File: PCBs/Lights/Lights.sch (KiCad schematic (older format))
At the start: 6 parts

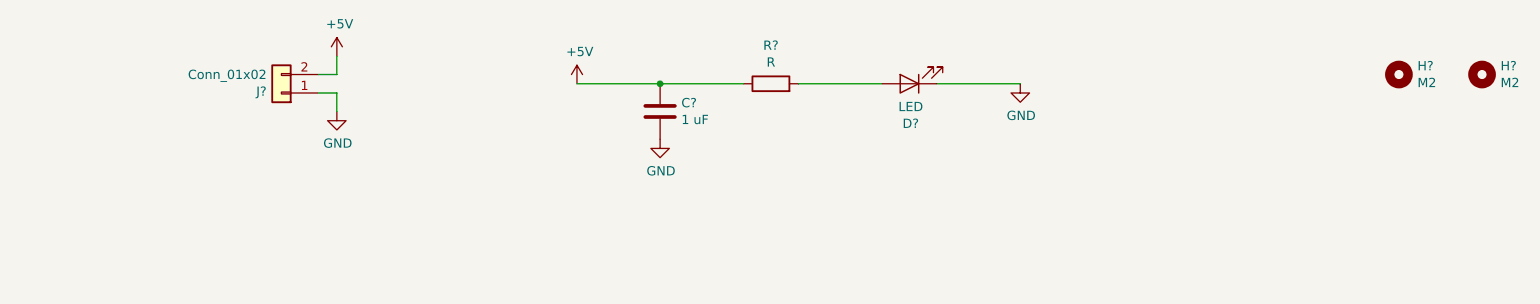
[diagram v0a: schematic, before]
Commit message: Schematic done
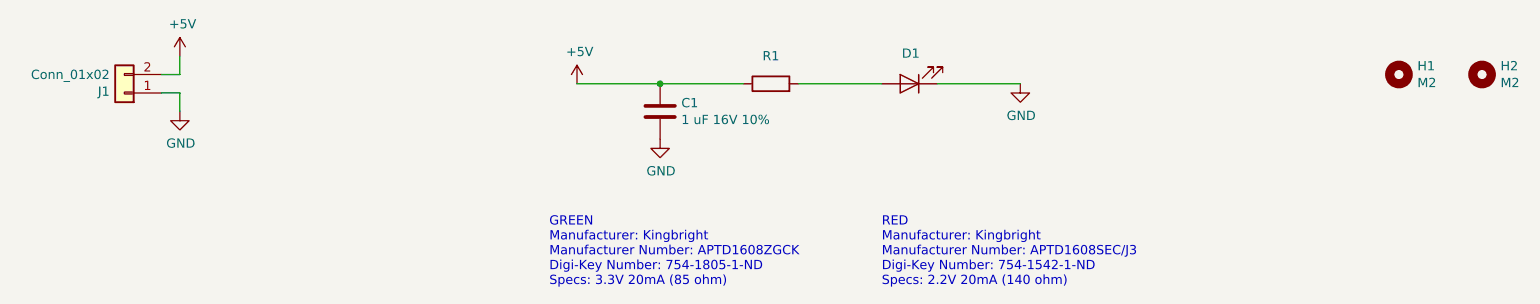
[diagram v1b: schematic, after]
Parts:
- C1: renamed from C?; value 1 uF -> 1 uF 16V 10%; footprint (none) -> Capacitor_SMD:C_0603_1608Metric_Pad1.05x0.95mm_HandSolder
- D1: renamed from D?; value LED -> See Notes; footprint (none) -> LED_SMD:LED_0603_1608Metric_Pad1.05x0.95mm_HandSolder
- J1: renamed from J?; footprint (none) -> Connector_JST:JST_GH_BM02B-GHS-TBT_1x02-1MP_P1.25mm_Vertical; Digi-Key # (none) -> 455-1578-1-ND; Digi-Key LinkDigi LinkDigi-Key Link (none) -> https://www.digikey.ca/en/products/detail/jst-sales-america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; Manufacturer (none) -> JST Sales America Inc.; Manufacturer # (none) -> BM02B-GHS-TBT(LF)(SN)(N)
- R1: renamed from R?; value R -> See Notes; footprint (none) -> Resistor_SMD:R_0603_1608Metric_Pad1.05x0.95mm_HandSolder
- gave numbers to parts that had none: 2
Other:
- note added: "GREEN\nManufacturer: Kingbright\nManufacturer Number: APTD1608ZGCK\nDigi-Key Number: 754-1805-1-ND\nSpecs: 3.3V 20mA (85 ohm)"
- note added: "RED\nManufacturer: Kingbright\nManufacturer Number: APTD1608SEC/J3\nDigi-Key Number: 754-1542-1-ND\nSpecs: 2.2V 20mA (140 ohm)"
- moved on the sheet: J1
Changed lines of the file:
@@
 EESchema Schematic File Version 4
+LIBS:Lights-cache
 EELAYER 30 0
 EELAYER END
@@
 $EndDescr
 $Comp
-L Connector_Generic:Conn_01x02 J?
+L Connector_Generic:Conn_01x02 J1
 U 1 1 5FF23492
-P 2700 4350
-F 0 "J?" H 2780 4342 50  0000 L CNN
-F 1 "Conn_01x02" H 2780 4251 50  0000 L CNN
-F 2 "" H 2700 4350 50  0001 C CNN
-F 3 "~" H 2700 4350 50  0001 C CNN
-	1    2700 4350
+P 1850 4350
+F 0 "J1" H 1930 4342 50  0000 L CNN
+F 1 "Conn_01x02" H 1930 4251 50  0000 L CNN
+F 2 "Connector_JST:JST_GH_BM02B-GHS-TBT_1x02-1MP_P1.25mm_Vertical" H 1850 4350 50  0001 C CNN
+F 3 "~" H 1850 4350 50  0001 C CNN
+F 4 "JST Sales America Inc." H 1850 4350 50  0001 C CNN "Manufacturer"
+F 5 "BM02B-GHS-TBT(LF)(SN)(N)" H 1850 4350 50  0001 C CNN "Manufacturer #"
+F 6 "455-1578-1-ND" H 1850 4350 50  0001 C CNN "Digi-Key #"
+F 7 "https://www.digikey.ca/en/products/detail/jst-sales-america-inc/BM02B-GHS-TBT-LF-SN-N/807800" H 1850 4350 50  0001 C CNN "Digi-Key LinkDigi LinkDigi-Key Link"
+	1    1850 4350
 	-1   0    0    1
 $EndComp
 $Comp
-L Device:R R?
+L Device:R R1
 U 1 1 5FF23AEE
 P 5350 4300
-F 0 "R?" V 5557 4300 50  0000 C CNN
-F 1 "R" V 5466 4300 50  0000 C CNN
-F 2 "" V 5280 4300 50  0001 C CNN
+F 0 "R1" V 5500 4300 50  0000 C CNN
+F 1 "See Notes" V 5466 4300 50  0001 C CNN
+F 2 "Resistor_SMD:R_0603_1608Metric_Pad1.05x0.95mm_HandSolder" V 5280 4300 50  0001 C CNN
 F 3 "~" H 5350 4300 50  0001 C CNN
 	1    5350 4300
@@
 $EndComp
 $Comp
-L Device:C C?
+L Device:C C1
 U 1 1 5FF23E80
 P 4750 4450
-F 0 "C?" H 4865 4496 50  0000 L CNN
-F 1 "1 uF" H 4865 4405 50  0000 L CNN
-F 2 "" H 4788 4300 50  0001 C CNN
+F 0 "C1" H 4865 4496 50  0000 L CNN
+F 1 "1 uF 16V 10%" H 4865 4405 50  0000 L CNN
+F 2 "Capacitor_SMD:C_0603_1608Metric_Pad1.05x0.95mm_HandSolder" H 4788 4300 50  0001 C CNN
 F 3 "~" H 4750 4450 50  0001 C CNN
 	1    4750 4450
@@
 $EndComp
 $Comp
-L Device:LED D?
+L Device:LED D1
 U 1 1 5FF24B5C
 P 6100 4300
-F 0 "D?" H 6093 4516 50  0000 C CNN
-F 1 "LED" H 6093 4425 50  0000 C CNN
-F 2 "" H 6100 4300 50  0001 C CNN
+F 0 "D1" H 6093 4136 50  0000 C CNN
+F 1 "See Notes" H 6093 4136 50  0001 C CNN
+F 2 "LED_SMD:LED_0603_1608Metric_Pad1.05x0.95mm_HandSolder" H 6100 4300 50  0001 C CNN
 F 3 "~" H 6100 4300 50  0001 C CNN
 	1    6100 4300
@@
 $EndComp
 $Comp
-L Mechanical:MountingHole H?
+L Mechanical:MountingHole H1
 U 1 1 5FF271A0
 P 8750 4250
-F 0 "H?" H 8850 4296 50  0000 L CNN
+F 0 "H1" H 8850 4296 50  0000 L CNN
 F 1 "M2" H 8850 4205 50  0000 L CNN
 F 2 "MountingHole:MountingHole_2.2mm_M2_ISO14580_Pad" H 8750 4250 50  0001 C CNN
@@
 $EndComp
 $Comp
-L power:GND #PWR?
+L power:GND #PWR0101
 U 1 1 5FF27C72
 P 6700 4300
-F 0 "#PWR?" H 6700 4050 50  0001 C CNN
+F 0 "#PWR0101" H 6700 4050 50  0001 C CNN
 F 1 "GND" H 6705 4127 50  0000 C CNN
 F 2 "" H 6700 4300 50  0001 C CNN
@@
 $EndComp
 $Comp
-L power:+5V #PWR?
+L power:+5V #PWR0102
 U 1 1 5FF2849B
-P 3000 4150
-F 0 "#PWR?" H 3000 4000 50  0001 C CNN
-F 1 "+5V" H 3015 4323 50  0000 C CNN
-F 2 "" H 3000 4150 50  0001 C CNN
-F 3 "" H 3000 4150 50  0001 C CNN
-	1    3000 4150
+P 2150 4150
+F 0 "#PWR0102" H 2150 4000 50  0001 C CNN
+F 1 "+5V" H 2165 4323 50  0000 C CNN
+F 2 "" H 2150 4150 50  0001 C CNN
+F 3 "" H 2150 4150 50  0001 C CNN
+	1    2150 4150
 	1    0    0    -1
 $EndComp
 Wire Wire Line
-	2900 4350 3000 4350
+	2050 4350 2150 4350
 Wire Wire Line
-	2900 4250 3000 4250
+	2050 4250 2150 4250
 Wire Wire Line
-	3000 4250 3000 4150
+	2150 4250 2150 4150
 Wire Wire Line
-	3000 4350 3000 4450
+	2150 4350 2150 4450
 $Comp
-L power:GND #PWR?
+L power:GND #PWR0103
 U 1 1 5FF33173
-P 3000 4450
-F 0 "#PWR?" H 3000 4200 50  0001 C CNN
-F 1 "GND" H 3005 4277 50  0000 C CNN
-F 2 "" H 3000 4450 50  0001 C CNN
-F 3 "" H 3000 4450 50  0001 C CNN
-	1    3000 4450
+P 2150 4450
+F 0 "#PWR0103" H 2150 4200 50  0001 C CNN
+F 1 "GND" H 2155 4277 50  0000 C CNN
+F 2 "" H 2150 4450 50  0001 C CNN
+F 3 "" H 2150 4450 50  0001 C CNN
+	1    2150 4450
 	1    0    0    -1
 $EndComp
@@
 	4300 4300 4750 4300
 $Comp
-L power:GND #PWR?
+L power:GND #PWR0104
 U 1 1 5FF3A0DA
 P 4750 4600
-F 0 "#PWR?" H 4750 4350 50  0001 C CNN
+F 0 "#PWR0104" H 4750 4350 50  0001 C CNN
 F 1 "GND" H 4755 4427 50  0000 C CNN
 F 2 "" H 4750 4600 50  0001 C CNN
@@
 $EndComp
 $Comp
-L power:+5V #PWR?
+L power:+5V #PWR0105
 U 1 1 5FF3A683
 P 4300 4300
-F 0 "#PWR?" H 4300 4150 50  0001 C CNN
+F 0 "#PWR0105" H 4300 4150 50  0001 C CNN
 F 1 "+5V" H 4315 4473 50  0000 C CNN
 F 2 "" H 4300 4300 50  0001 C CNN
@@
 Connection ~ 4750 4300
 $Comp
-L Mechanical:MountingHole H?
+L Mechanical:MountingHole H2
 U 1 1 5FF4097E
 P 9200 4250
-F 0 "H?" H 9300 4296 50  0000 L CNN
+F 0 "H2" H 9300 4296 50  0000 L CNN
 F 1 "M2" H 9300 4205 50  0000 L CNN
 F 2 "MountingHole:MountingHole_2.2mm_M2_ISO14580_Pad" H 9200 4250 50  0001 C CNN
@@
 	1    0    0    -1
 $EndComp
+Text Notes 4150 5400 0    50   ~ 0
+GREEN\nManufacturer: Kingbright\nManufacturer Number: APTD1608ZGCK\nDigi-Key Number: 754-1805-1-ND\nSpecs: 3.3V 20mA (85 ohm)
+Text Notes 5950 5400 0    50   ~ 0
+RED\nManufacturer: Kingbright\nManufacturer Number: APTD1608SEC/J3\nDigi-Key Number: 754-1542-1-ND\nSpecs: 2.2V 20mA (140 ohm)
 $EndSCHEMATC

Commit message: board complete
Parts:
- J1: footprint Connector_JST:JST_GH_BM02B-GHS-TBT_1x02-1MP_P1.25mm_Vertical -> Connector_JST:JST_GH_SM02B-GHS-TB_1x02-1MP_P1.25mm_Horizontal; Digi-Key # 455-1578-1-ND -> 455-1564-1-ND; Digi-Key LinkDigi LinkDigi-Key Link https://www.digikey.ca/en/products/detail/jst-sales-america-inc/BM02B-GHS-TBT-LF-SN-N/807800 -> https://www.digikey.ca/en/products/detail/jst-sales-america-inc/SM02B-GHS-TB-LF-SN/807786?s=N4IgTCBcDaIMoFkAMYBCBaA4gCTiAugL5A; Manufacturer # BM02B-GHS-TBT(LF)(SN)(N) -> SM02B-GHS-TB(LF)(SN)
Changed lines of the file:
@@
 F 0 "J1" H 1930 4342 50  0000 L CNN
 F 1 "Conn_01x02" H 1930 4251 50  0000 L CNN
-F 2 "Connector_JST:JST_GH_BM02B-GHS-TBT_1x02-1MP_P1.25mm_Vertical" H 1850 4350 50  0001 C CNN
+F 2 "Connector_JST:JST_GH_SM02B-GHS-TB_1x02-1MP_P1.25mm_Horizontal" H 1850 4350 50  0001 C CNN
 F 3 "~" H 1850 4350 50  0001 C CNN
 F 4 "JST Sales America Inc." H 1850 4350 50  0001 C CNN "Manufacturer"
-F 5 "BM02B-GHS-TBT(LF)(SN)(N)" H 1850 4350 50  0001 C CNN "Manufacturer #"
-F 6 "455-1578-1-ND" H 1850 4350 50  0001 C CNN "Digi-Key #"
-F 7 "https://www.digikey.ca/en/products/detail/jst-sales-america-inc/BM02B-GHS-TBT-LF-SN-N/807800" H 1850 4350 50  0001 C CNN "Digi-Key LinkDigi LinkDigi-Key Link"
+F 5 "SM02B-GHS-TB(LF)(SN)" H 1850 4350 50  0001 C CNN "Manufacturer #"
+F 6 "455-1564-1-ND" H 1850 4350 50  0001 C CNN "Digi-Key #"
+F 7 "https://www.digikey.ca/en/products/detail/jst-sales-america-inc/SM02B-GHS-TB-LF-SN/807786?s=N4IgTCBcDaIMoFkAMYBCBaA4gCTiAugL5A" H 1850 4350 50  0001 C CNN "Digi-Key LinkDigi LinkDigi-Key Link"
 	1    1850 4350
 	-1   0    0    1
